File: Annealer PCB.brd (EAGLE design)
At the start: 53.3 x 77.5 mm, 34 parts

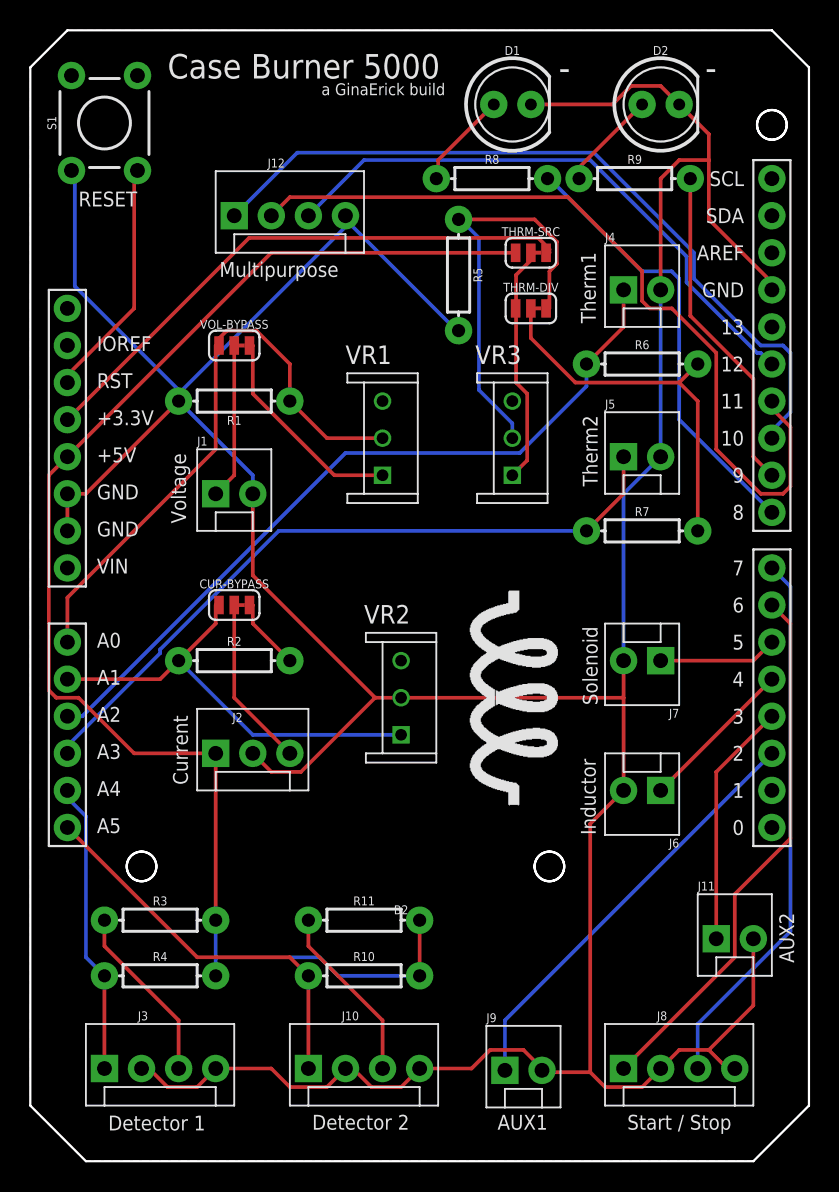
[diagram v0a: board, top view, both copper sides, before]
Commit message: Added I2C for an LCD or similar
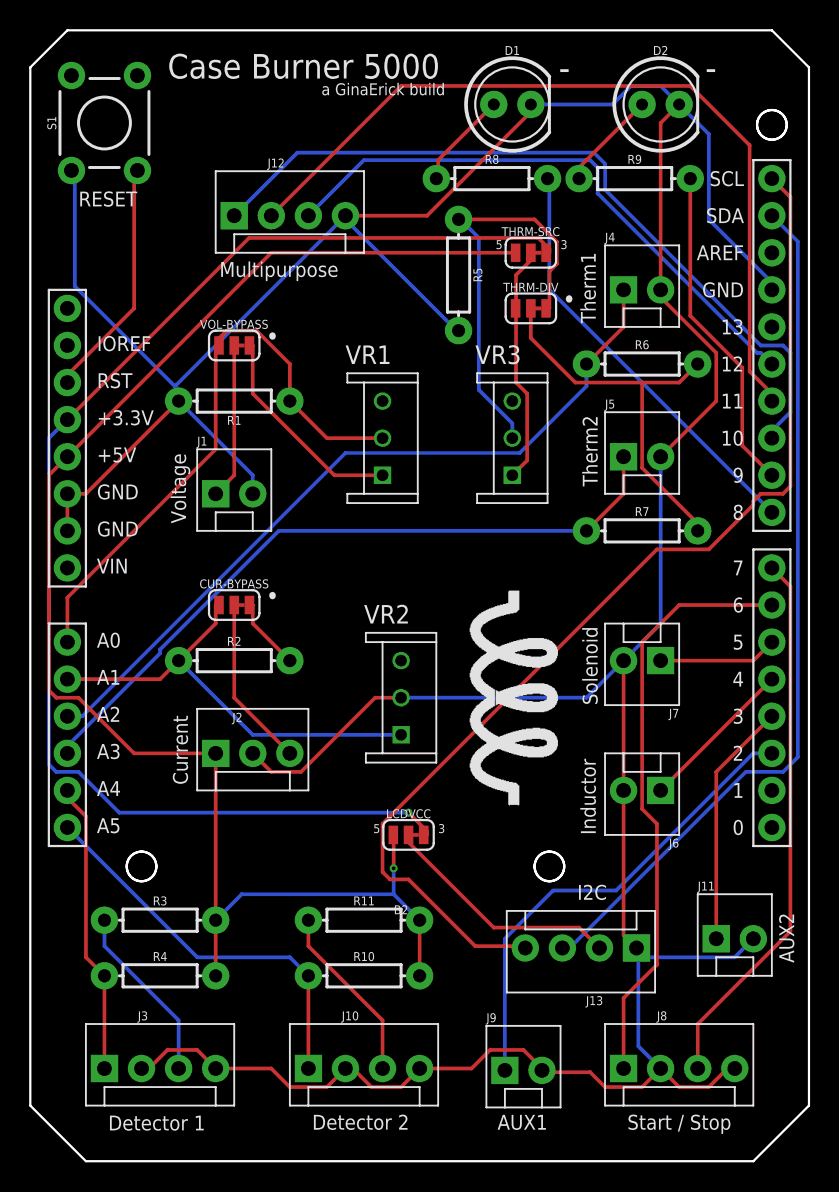
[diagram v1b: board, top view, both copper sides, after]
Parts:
- added J13: (no value), SparkFun-Connectors:MOLEX-1X4
- added LCDVCC: JUMPER-SMT_3_1-NC_TRACE_SILK, SparkFun-Jumpers:SMT-JUMPER_3_1-NC_TRACE_SILK
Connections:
- new net N$12: J13.2, LCDVCC.2
- new net SCL: B2.SCL, J13.4
- new net SDA: B2.SDA, J13.3
- net 3.3V: now also LCDVCC.3
- net 5V: now also LCDVCC.1
- net GND: now also J13.1
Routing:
- net SCL: track 0.00 -> 74.5 mm
- net SDA: track 0.00 -> 59.4 mm
- net 3.3V: track 39.0 -> 91.4 mm, vias 0 -> 1
- net N$12: track 0.00 -> 16.6 mm
- net 5V: track 99.8 -> 104.8 mm, vias 0 -> 1
- net GND: track 263.5 -> 267.6 mm
- net D6: track 37.0 -> 40.5 mm
- net D2: track 29.3 -> 32.6 mm
- net D8: track 30.5 -> 29.3 mm
- net N$1: track 25.9 -> 27.0 mm
- removed copper zone on layer 1, net GND
- removed copper zone on layer 16, net GND
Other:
- board text added: "3"
- board text added: "5"
- board text added: "I2C"
- board text added: "•"

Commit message: Swap pins on thermistor2 and prox2
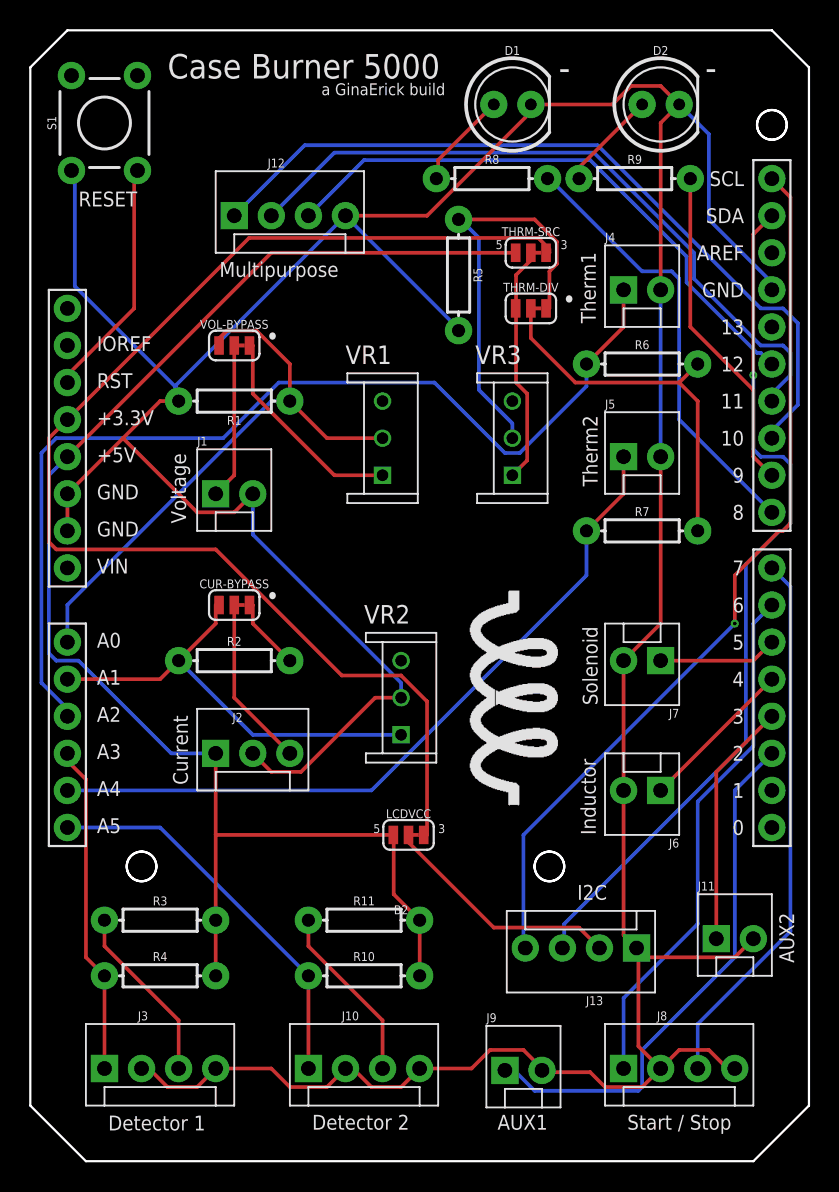
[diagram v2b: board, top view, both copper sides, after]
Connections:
- net A3: now also J3.1, R4.P$1; no longer J5.1, R7.P$1
- net A4: now also J5.1, R7.P$1; no longer J3.1, R4.P$1
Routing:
- net A4: track 20.1 -> 50.8 mm
- net A3: track 48.5 -> 22.6 mm
- net A2: track 52.6 -> 69.7 mm
- net SCL: track 74.5 -> 61.0 mm, vias 0 -> 1
- net D11: track 56.3 -> 47.9 mm
- net D6: track 40.5 -> 36.0 mm
- net D2: track 32.6 -> 36.7 mm
- net 3.3V: track 91.4 -> 87.7 mm, vias 1 -> 0
- net 5V: track 104.8 -> 102.6 mm, vias 1 -> 0
- net GND: track 267.6 -> 269.7 mm
- net D10: track 53.0 -> 54.3 mm
- net A0: track 41.2 -> 40.0 mm
- net D8: track 29.3 -> 30.5 mm
- net N$1: track 27.0 -> 25.9 mm
- net SDA: track 59.4 -> 59.3 mm, vias 0 -> 1
